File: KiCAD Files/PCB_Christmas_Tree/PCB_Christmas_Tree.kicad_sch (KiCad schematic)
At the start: 69 parts, among them J1 Conn_01x03_Pin, J2 CR2032, J3 Conn_01x05_Pin, J4 Conn_01x05_Pin, J5 Conn_01x05_Pin, J6 Conn_01x05_Pin, Q1 PMOS, Q2 PMOS, Q3 PMOS, Q4 NPN, Q5 PMOS, Q6 PMOS, SW1 SW_Omron_B3FS, U1 ATtiny402-SS

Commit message: schematic revision
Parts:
- removed J3, J4, J5, J6: Conn_01x05_Pin, LocalFootprintLib:Multi_board_connector, symbol Connector:Conn_01x05_Pin
- removed Q6: PMOS, Package_TO_SOT_SMD:SOT-323_SC-70_Handsoldering, symbol Simulation_SPICE:PMOS
- removed R6: 1k, Resistor_SMD:R_0603_1608Metric_Pad0.98x0.95mm_HandSolder, symbol Device:R
- added J3, J4, J5, J7: Conn_01x04_Pin, LocalFootprintLib:Multi_board_connector, symbol Connector:Conn_01x04_Pin
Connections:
- net LED_Set_4 is gone; now on net LED_Set_3: U1.3 (PA7)
- net GND: now also J3.4 (Pin_4), J4.4 (Pin_4), J5.4 (Pin_4), J7.4 (Pin_4)
- net LED_Power_1: now also D11.2 (A), D13.2 (A), J3.1 (Pin_1), J4.1 (Pin_1), J5.1 (Pin_1), J7.1 (Pin_1)
- net LED_Power_2: now also D15.2 (A), D17.2 (A), J3.2 (Pin_2), J4.2 (Pin_2), J5.2 (Pin_2), J7.2 (Pin_2)
- net LED_Power_3: now also D20.2 (A), D24.2 (A), J3.3 (Pin_3), J4.3 (Pin_3), J5.3 (Pin_3), J7.3 (Pin_3)
- net Switch_in: no longer J1.2 (Pin_2), U1.6 (~{RESET}/PA0)
- removed net LED_Power_4: D11.2 (A), D13.2 (A), D15.2 (A), D17.2 (A), D20.2 (A), D24.2 (A)
- new net UDPI: J1.2 (Pin_2), U1.6 (~{RESET}/PA0)

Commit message: pcb revision
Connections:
- net LED_Set_3: no longer U1.3 (PA7)
- net Switch_in: now also U1.3 (PA7)
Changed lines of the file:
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@@
+    (effects (font (size 1.27 1.27)) (justify left bottom))
+  )
+  (label "Switch_in" (at 146.05 54.61 0) (fields_autoplaced)
     (effects (font (size 1.27 1.27)) (justify left bottom))
   )
@@
     (effects (font (size 1.27 1.27)) (justify left bottom))
   )
-  (label "LED_Set_3" (at 146.05 54.61 0) (fields_autoplaced)
-    (effects (font (size 1.27 1.27)) (justify left bottom))
-  )

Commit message: schematic update, footprint revision
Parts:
- removed Q1, Q2, Q3, Q5: PMOS, Package_TO_SOT_SMD:SOT-323_SC-70_Handsoldering, symbol Simulation_SPICE:PMOS
- removed Q4: NPN, Package_TO_SOT_SMD:SOT-23, symbol Simulation_SPICE:NPN
- added Q1, Q2, Q3, Q5: AO3401A, Package_TO_SOT_SMD:SOT-23, symbol Transistor_FET:AO3401A
- added Q4: BC817, Package_TO_SOT_SMD:SOT-23, symbol Transistor_BJT:BC817
- R1: value 100k -> 10k
- R2, R5: value 1k -> 10k
- Rq1: renamed from R3; value 1k -> 10k
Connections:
- net +BATT: now also Q1.2 (S)
- net GND: now also Q4.2 (E)
- net LED_Power_1: now also Q3.3 (D)
- net LED_Power_2: now also Q5.3 (D)
- net LED_Power_3: now also Q2.3 (D)
- net LED_Set_3: now also U1.4 (PA1); no longer U1.2 (PA6)
- net Power_sustain: now also U1.2 (PA6); no longer U1.4 (PA1)
- net VDD: now also Q1.3 (D), Q2.2 (S), Q3.2 (S), Q5.2 (S)
- net at R2.2: now also Q2.1 (G)
- net at D1.1 (A), R1.2: now also Q1.1 (G), Q4.3 (C)
- net at Rq1.2: now also Q3.1 (G)
- net at R5.2: now also Q5.1 (G)
- net at R4.1: now also Q4.1 (B)
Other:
- note removed: "NOTES: - check if the attiny has internal pullup for switch input - check the led currents"

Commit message: v2 added
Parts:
- Q1: renamed from Q2; footprint Package_TO_SOT_SMD:SOT-23 -> Package_TO_SOT_SMD:SOT-323_SC-70_Handsoldering
- Q2: renamed from Q3; footprint Package_TO_SOT_SMD:SOT-23 -> Package_TO_SOT_SMD:SOT-323_SC-70_Handsoldering
- Q3: renamed from Q1; footprint Package_TO_SOT_SMD:SOT-23 -> Package_TO_SOT_SMD:SOT-323_SC-70_Handsoldering
- Q5: footprint Package_TO_SOT_SMD:SOT-23 -> Package_TO_SOT_SMD:SOT-323_SC-70_Handsoldering
- renumbered D6 to D10, D7 to D11, D8 to D12, D9 to D13, D10 to D14, D11 to D15, D12 to D16, D13 to D17, D14 to D18, D15 to D19, D23 to D2, D16 to D20, D17 to D21, D19 to D22, D20 to D23, D25 to D24, D24 to D25, D22 to D3, D21 to D4, D18 to D5, D2 to D6, D3 to D7, D4 to D8, D5 to D9, J2 to J1, J1 to J2, J7 to J3, J3 to J5, J5 to J6, R2 to R1, R7 to R10, R8 to R11, R9 to R12, R10 to R13, R11 to R14, R12 to R15, R13 to R16, R14 to R17, R15 to R18, R16 to R19, Rq1 to R2, R17 to R20, R18 to R21, R19 to R22, R20 to R23, R21 to R24, R22 to R25, R24 to R26, R25 to R27, R30 to R28, R1 to R3, R28 to R6, R27 to R7, R26 to R8, R23 to R9
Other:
- company: Krzysztof Sikora -> AGH University of Krakow
- moved on the sheet: D1, D10, D11, D12, D13, D14, D15, D16, D17, D18, D19, D2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

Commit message: PCB update
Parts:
- R1, R10, R11, R12, R13, R14, R15, R16, R17, R18, R19, R2, R20, R21, R22, R23, R24, R25, R26, R27, R28, R29, R3, R4, R5, R6, R7, R8, R9: footprint Resistor_SMD:R_0603_1608Metric_Pad0.98x0.95mm_HandSolder -> Resistor_SMD:R_0805_2012Metric_Pad1.20x1.40mm_HandSolder
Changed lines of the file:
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@@
       (effects (font (size 1.27 1.27)) (justify left))
     )
-    (property "Footprint" "Resistor_SMD:R_0603_1608Metric_Pad0.98x0.95mm_HandSolder" (at 217.678 148.59 90)
+    (property "Footprint" "Resistor_SMD:R_0805_2012Metric_Pad1.20x1.40mm_HandSolder" (at 217.678 148.59 90)
       (effects (font (size 1.27 1.27)) hide)
     )
@@
       (effects (font (size 1.27 1.27)) (justify left))
     )
-    (property "Footprint" "Resistor_SMD:R_0603_1608Metric_Pad0.98x0.95mm_HandSolder" (at 228.473 103.505 90)
+    (property "Footprint" "Resistor_SMD:R_0805_2012Metric_Pad1.20x1.40mm_HandSolder" (at 228.473 103.505 90)
       (effects (font (size 1.27 1.27)) hide)
     )
@@
       (effects (font (size 1.27 1.27)) (justify left))
     )
-    (property "Footprint" "Resistor_SMD:R_0603_1608Metric_Pad0.98x0.95mm_HandSolder" (at 185.928 104.775 90)
+    (property "Footprint" "Resistor_SMD:R_0805_2012Metric_Pad1.20x1.40mm_HandSolder" (at 185.928 104.775 90)
       (effects (font (size 1.27 1.27)) hide)
     )
@@
       (effects (font (size 1.27 1.27)) (justify left))
     )
-    (property "Footprint" "Resistor_SMD:R_0603_1608Metric_Pad0.98x0.95mm_HandSolder" (at 37.465 135.382 90)
+    (property "Footprint" "Resistor_SMD:R_0805_2012Metric_Pad1.20x1.40mm_HandSolder" (at 37.465 135.382 90)
       (effects (font (size 1.27 1.27)) hide)
     )
@@
       (effects (font (size 1.27 1.27)) (justify left))
     )
-    (property "Footprint" "Resistor_SMD:R_0603_1608Metric_Pad0.98x0.95mm_HandSolder" (at 46.228 40.005 90)
+    (property "Footprint" "Resistor_SMD:R_0805_2012Metric_Pad1.20x1.40mm_HandSolder" (at 46.228 40.005 90)
       (effects (font (size 1.27 1.27)) hide)
     )
@@
       (effects (font (size 1.27 1.27)) (justify left))
     )
-    (property "Footprint" "Resistor_SMD:R_0603_1608Metric_Pad0.98x0.95mm_HandSolder" (at 267.843 147.955 90)
+    (property "Footprint" "Resistor_SMD:R_0805_2012Metric_Pad1.20x1.40mm_HandSolder" (at 267.843 147.955 90)
       (effects (font (size 1.27 1.27)) hide)
     )
@@
       (effects (font (size 1.27 1.27)) (justify left))
     )
-    (property "Footprint" "Resistor_SMD:R_0603_1608Metric_Pad0.98x0.95mm_HandSolder" (at 197.993 149.225 90)
+    (property "Footprint" "Resistor_SMD:R_0805_2012Metric_Pad1.20x1.40mm_HandSolder" (at 197.993 149.225 90)
       (effects (font (size 1.27 1.27)) hide)
     )
@@
       (effects (font (size 1.27 1.27)) (justify left))
     )
-    (property "Footprint" "Resistor_SMD:R_0603_1608Metric_Pad0.98x0.95mm_HandSolder" (at 165.608 149.86 90)
+    (property "Footprint" "Resistor_SMD:R_0805_2012Metric_Pad1.20x1.40mm_HandSolder" (at 165.608 149.86 90)
       (effects (font (size 1.27 1.27)) hide)
     )
@@
       (effects (font (size 1.27 1.27)) (justify left))
     )
-    (property "Footprint" "Resistor_SMD:R_0603_1608Metric_Pad0.98x0.95mm_HandSolder" (at 238.633 103.505 90)
+    (property "Footprint" "Resistor_SMD:R_0805_2012Metric_Pad1.20x1.40mm_HandSolder" (at 238.633 103.505 90)
       (effects (font (size 1.27 1.27)) hide)
     )
@@
       (effects (font (size 1.27 1.27)) (justify left))
     )
-    (property "Footprint" "Resistor_SMD:R_0603_1608Metric_Pad0.98x0.95mm_HandSolder" (at 267.843 103.505 90)
+    (property "Footprint" "Resistor_SMD:R_0805_2012Metric_Pad1.20x1.40mm_HandSolder" (at 267.843 103.505 90)
       (effects (font (size 1.27 1.27)) hide)
     )
@@
       (effects (font (size 1.27 1.27)) (justify left))
     )
-    (property "Footprint" "Resistor_SMD:R_0603_1608Metric_Pad0.98x0.95mm_HandSolder" (at 187.833 149.86 90)
+    (property "Footprint" "Resistor_SMD:R_0805_2012Metric_Pad1.20x1.40mm_HandSolder" (at 187.833 149.86 90)
       (effects (font (size 1.27 1.27)) hide)
     )
@@
       (effects (font (size 1.27 1.27)) (justify left))
     )
-    (property "Footprint" "Resistor_SMD:R_0603_1608Metric_Pad0.98x0.95mm_HandSolder" (at 176.403 149.86 90)
+    (property "Footprint" "Resistor_SMD:R_0805_2012Metric_Pad1.20x1.40mm_HandSolder" (at 176.403 149.86 90)
       (effects (font (size 1.27 1.27)) hide)
     )
@@
       (effects (font (size 1.27 1.27)) (justify left))
     )
-    (property "Footprint" "Resistor_SMD:R_0603_1608Metric_Pad0.98x0.95mm_HandSolder" (at 217.678 104.14 90)
+    (property "Footprint" "Resistor_SMD:R_0805_2012Metric_Pad1.20x1.40mm_HandSolder" (at 217.678 104.14 90)
       (effects (font (size 1.27 1.27)) hide)
     )
@@
       (effects (font (size 1.27 1.27)) (justify left))
     )
-    (property "Footprint" "Resistor_SMD:R_0603_1608Metric_Pad0.98x0.95mm_HandSolder" (at 258.318 103.505 90)
+    (property "Footprint" "Resistor_SMD:R_0805_2012Metric_Pad1.20x1.40mm_HandSolder" (at 258.318 103.505 90)
       (effects (font (size 1.27 1.27)) hide)
     )
@@
       (effects (font (size 1.27 1.27)) (justify left))
     )
-    (property "Footprint" "Resistor_SMD:R_0603_1608Metric_Pad0.98x0.95mm_HandSolder" (at 228.473 147.955 90)
+    (property "Footprint" "Resistor_SMD:R_0805_2012Metric_Pad1.20x1.40mm_HandSolder" (at 228.473 147.955 90)
       (effects (font (size 1.27 1.27)) hide)
     )
@@
       (effects (font (size 1.27 1.27)) (justify left))
     )
-    (property "Footprint" "Resistor_SMD:R_0603_1608Metric_Pad0.98x0.95mm_HandSolder" (at 248.158 147.955 90)
+    (property "Footprint" "Resistor_SMD:R_0805_2012Metric_Pad1.20x1.40mm_HandSolder" (at 248.158 147.955 90)
       (effects (font (size 1.27 1.27)) hide)
     )
@@
       (effects (font (size 1.27 1.27)) (justify left))
     )
-    (property "Footprint" "Resistor_SMD:R_0603_1608Metric_Pad0.98x0.95mm_HandSolder" (at 143.383 149.225 90)
+    (property "Footprint" "Resistor_SMD:R_0805_2012Metric_Pad1.20x1.40mm_HandSolder" (at 143.383 149.225 90)
       (effects (font (size 1.27 1.27)) hide)
     )
@@
       (effects (font (size 1.27 1.27)) (justify left))
     )
-    (property "Footprint" "Resistor_SMD:R_0603_1608Metric_Pad0.98x0.95mm_HandSolder" (at 36.83 171.577 90)
+    (property "Footprint" "Resistor_SMD:R_0805_2012Metric_Pad1.20x1.40mm_HandSolder" (at 36.83 171.577 90)
       (effects (font (size 1.27 1.27)) hide)
     )
@@
       (effects (font (size 1.27 1.27)) (justify left))
     )
-    (property "Footprint" "Resistor_SMD:R_0603_1608Metric_Pad0.98x0.95mm_HandSolder" (at 175.768 105.41 90)
+    (property "Footprint" "Resistor_SMD:R_0805_2012Metric_Pad1.20x1.40mm_HandSolder" (at 175.768 105.41 90)
       (effects (font (size 1.27 1.27)) hide)
     )
@@
       (effects (font (size 1.27 1.27)) (justify left))
     )
-    (property "Footprint" "Resistor_SMD:R_0603_1608Metric_Pad0.98x0.95mm_HandSolder" (at 258.318 147.955 90)
+    (property "Footprint" "Resistor_SMD:R_0805_2012Metric_Pad1.20x1.40mm_HandSolder" (at 258.318 147.955 90)
       (effects (font (size 1.27 1.27)) hide)
     )
@@
       (effects (font (size 1.27 1.27)) (justify left))
     )
-    (property "Footprint" "Resistor_SMD:R_0603_1608Metric_Pad0.98x0.95mm_HandSolder" (at 154.813 149.86 90)
+    (property "Footprint" "Resistor_SMD:R_0805_2012Metric_Pad1.20x1.40mm_HandSolder" (at 154.813 149.86 90)
       (effects (font (size 1.27 1.27)) hide)
     )
@@
       (effects (font (size 1.27 1.27)) (justify left))
     )
-    (property "Footprint" "Resistor_SMD:R_0603_1608Metric_Pad0.98x0.95mm_HandSolder" (at 155.448 105.41 90)
+    (property "Footprint" "Resistor_SMD:R_0805_2012Metric_Pad1.20x1.40mm_HandSolder" (at 155.448 105.41 90)
       (effects (font (size 1.27 1.27)) hide)
     )
@@
       (effects (font (size 1.27 1.27)) (justify left))
     )
-    (property "Footprint" "Resistor_SMD:R_0603_1608Metric_Pad0.98x0.95mm_HandSolder" (at 248.158 103.505 90)
+    (property "Footprint" "Resistor_SMD:R_0805_2012Metric_Pad1.20x1.40mm_HandSolder" (at 248.158 103.505 90)
       (effects (font (size 1.27 1.27)) hide)
     )
@@
       (effects (font (size 1.27 1.27)) (justify left))
     )
-    (property "Footprint" "Resistor_SMD:R_0603_1608Metric_Pad0.98x0.95mm_HandSolder" (at 196.088 104.14 90)
+    (property "Footprint" "Resistor_SMD:R_0805_2012Metric_Pad1.20x1.40mm_HandSolder" (at 196.088 104.14 90)
       (effects (font (size 1.27 1.27)) hide)
     )
@@
       (effects (font (size 1.27 1.27)) (justify left))
     )
-    (property "Footprint" "Resistor_SMD:R_0603_1608Metric_Pad0.98x0.95mm_HandSolder" (at 238.633 147.955 90)
+    (property "Footprint" "Resistor_SMD:R_0805_2012Metric_Pad1.20x1.40mm_HandSolder" (at 238.633 147.955 90)
       (effects (font (size 1.27 1.27)) hide)
     )
@@
       (effects (font (size 1.27 1.27)) (justify left))
     )
-    (property "Footprint" "Resistor_SMD:R_0603_1608Metric_Pad0.98x0.95mm_HandSolder" (at 76.835 134.747 90)
+    (property "Footprint" "Resistor_SMD:R_0805_2012Metric_Pad1.20x1.40mm_HandSolder" (at 76.835 134.747 90)
       (effects (font (size 1.27 1.27)) hide)
     )
@@
       (effects (font (size 1.27 1.27)) (justify left))
     )
-    (property "Footprint" "Resistor_SMD:R_0603_1608Metric_Pad0.98x0.95mm_HandSolder" (at 165.608 105.41 90)
+    (property "Footprint" "Resistor_SMD:R_0805_2012Metric_Pad1.20x1.40mm_HandSolder" (at 165.608 105.41 90)
       (effects (font (size 1.27 1.27)) hide)
     )
@@
       (effects (font (size 1.27 1.27)) (justify left))
     )
-    (property "Footprint" "Resistor_SMD:R_0603_1608Metric_Pad0.98x0.95mm_HandSolder" (at 144.018 105.41 90)
+    (property "Footprint" "Resistor_SMD:R_0805_2012Metric_Pad1.20x1.40mm_HandSolder" (at 144.018 105.41 90)
       (effects (font (size 1.27 1.27)) hide)
     )
@@
       (effects (font (size 1.27 1.27)))
     )
-    (property "Footprint" "Resistor_SMD:R_0603_1608Metric_Pad0.98x0.95mm_HandSolder" (at 73.66 79.248 90)
-      (effects (font (size 1.27 1.27)) hide)
-    )
+    (property "Footprint" "Resistor_SMD:R_0805_2012Metric_Pad1.20x1.40mm_HandSolder" (at 73.66 79.248 90)
+      (effects (font (size 1.27 1.27)) hide)
+    )

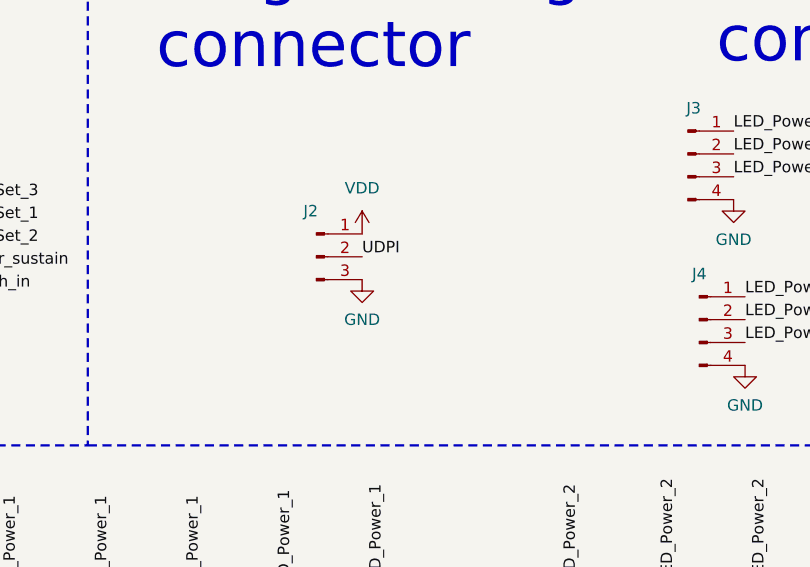
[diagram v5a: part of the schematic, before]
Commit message: zmiana pinoutu zlacza UPDI
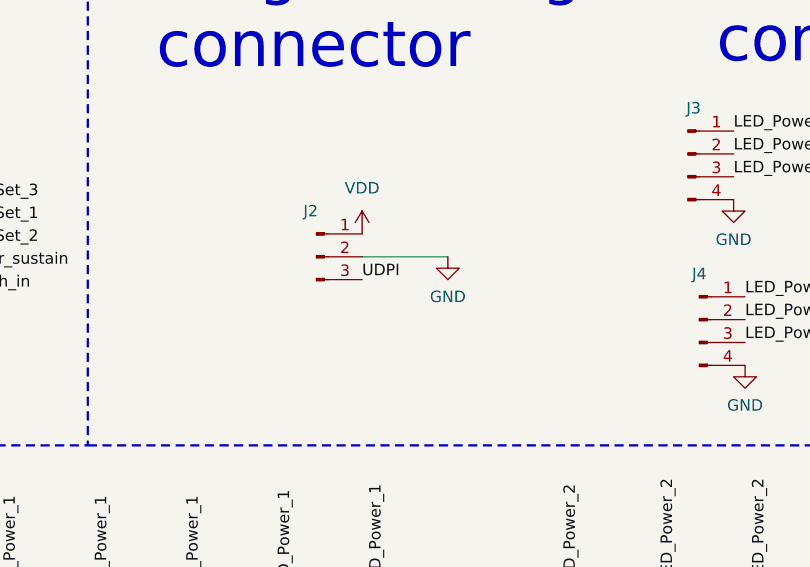
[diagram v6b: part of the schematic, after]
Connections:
- net GND: now also J2.2 (Pin_2); no longer J2.3 (Pin_3)
- net UDPI: now also J2.3 (Pin_3); no longer J2.2 (Pin_2)
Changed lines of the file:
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@@
+    (stroke (width 0) (type default))
+  )
+  (wire (pts (xy 191.77 50.165) (xy 201.295 50.165))
     (stroke (width 0) (type default))
   )
@@
     (effects (font (size 1.27 1.27)) (justify left bottom))
   )
-  (label "UDPI" (at 191.77 50.165 0) (fields_autoplaced)
+  (label "UDPI" (at 191.77 52.705 0) (fields_autoplaced)
     (effects (font (size 1.27 1.27)) (justify left bottom))
   )
@@
     )
   )
+  (symbol (lib_id "power:GND") (at 201.295 50.165 0) (unit 1)
+    (in_bom yes) (on_board yes) (dnp no) (fields_autoplaced)
+    (property "Reference" "#PWR022" (at 201.295 56.515 0)
+      (effects (font (size 1.27 1.27)) hide)
+    )
+    (property "Value" "GND" (at 201.295 54.61 0)
+      (effects (font (size 1.27 1.27)))
+    )
+    (property "Footprint" "" (at 201.295 50.165 0)
+      (effects (font (size 1.27 1.27)) hide)
+    )
+    (property "Datasheet" "" (at 201.295 50.165 0)
+      (effects (font (size 1.27 1.27)) hide)
+    )
+    (pin "1")
+    (instances
+      (project "PCB_Christmas_Tree"
+        (path "/e614f44a-b3b4-458d-ace1-aabdd8a54d37"
+          (reference "#PWR022") (unit 1)
+        )
+      )
+    )
+  )
   (symbol (lib_id "Device:LED") (at 184.15 94.615 90) (unit 1)
     (in_bom yes) (on_board yes) (dnp no) (fields_autoplaced)
@@
         )
       )
-    )
-  )
-  (symbol (lib_id "power:GND") (at 191.77 52.705 0) (unit 1)
-    (in_bom yes) (on_board yes) (dnp no) (fields_autoplaced)
-    (property "Reference" "#PWR022" (at 191.77 59.055 0)
-      (effects (font (size 1.27 1.27)) hide)
-    )
-    (property "Value" "GND" (at 191.77 57.15 0)
-      (effects (font (size 1.27 1.27)))
-    )
-    (property "Footprint" "" (at 191.77 52.705 0)
-      (effects (font (size 1.27 1.27)) hide)
-    )
-    (property "Datasheet" "" (at 191.77 52.705 0)
-      (effects (font (size 1.27 1.27)) hide)
-    )
-    (pin "1")
-    (instances
-      (project "PCB_Christmas_Tree"
-        (path "/e614f44a-b3b4-458d-ace1-aabdd8a54d37"
-          (reference "#PWR022") (unit 1)
-        )
-      )
